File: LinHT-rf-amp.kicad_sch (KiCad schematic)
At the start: 22 parts, among them J1 Conn_Coaxial, J2 Conn_Coaxial, U1 GRF5604

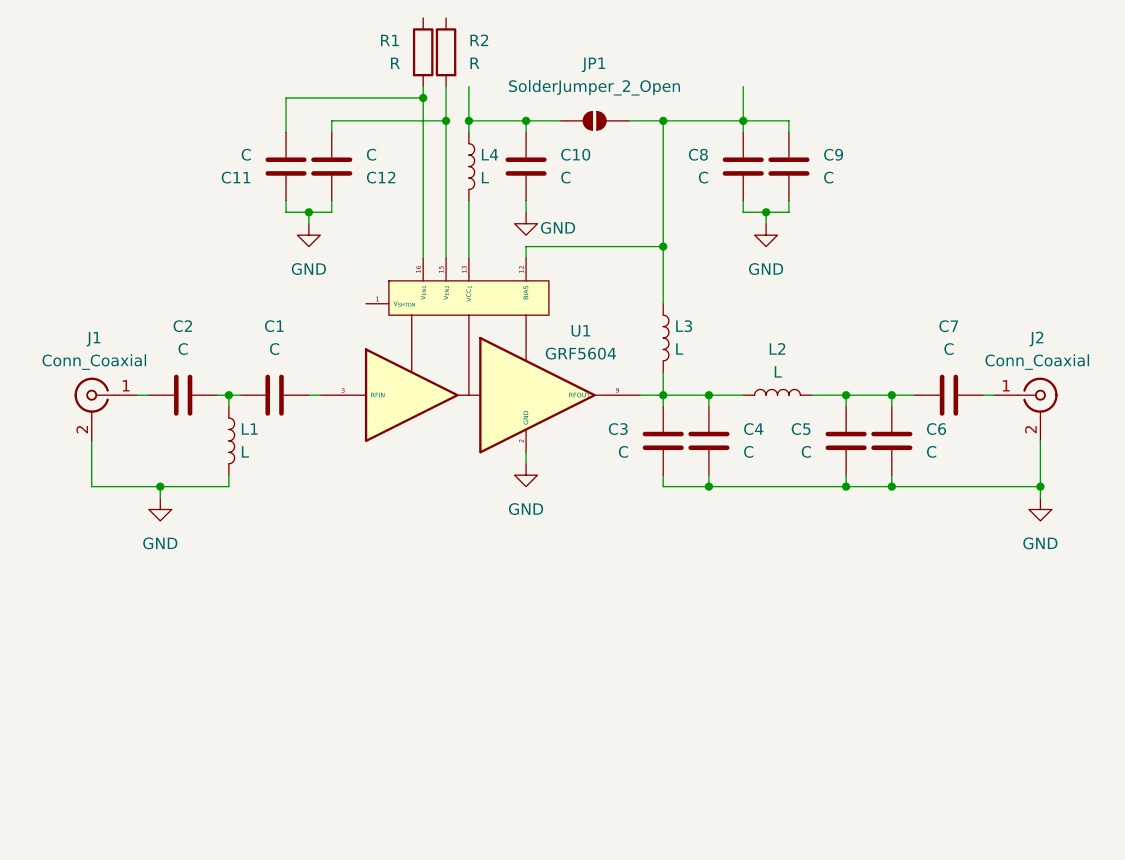
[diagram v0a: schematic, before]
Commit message: Added component values and connectors
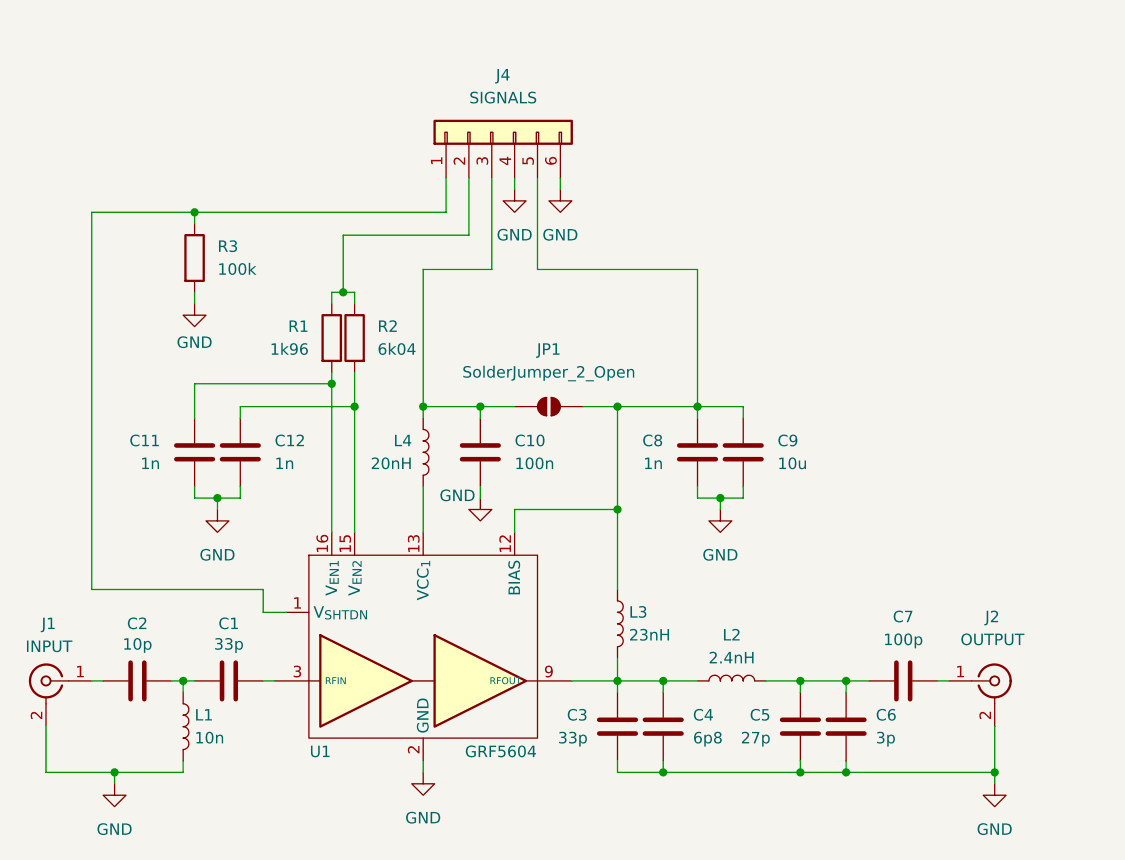
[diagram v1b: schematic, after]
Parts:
- added J4: SIGNALS, Connector_PinHeader_2.54mm:PinHeader_1x06_P2.54mm_Vertical, symbol Connector_Generic:Conn_01x06
- added R3: 100k, Resistor_SMD:R_0402_1005Metric, symbol Device:R
- C1, C3: value C -> 33p; footprint (none) -> Capacitor_SMD:C_0402_1005Metric
- C10: value C -> 100n; footprint (none) -> Capacitor_SMD:C_0402_1005Metric
- C11, C12, C8: value C -> 1n; footprint (none) -> Capacitor_SMD:C_0402_1005Metric
- C2: value C -> 10p; footprint (none) -> Capacitor_SMD:C_0402_1005Metric
- C4: value C -> 6p8; footprint (none) -> Capacitor_SMD:C_0402_1005Metric
- C5: value C -> 27p; footprint (none) -> Capacitor_SMD:C_0402_1005Metric
- C6: value C -> 3p; footprint (none) -> Capacitor_SMD:C_0402_1005Metric
- C7: value C -> 100p; footprint (none) -> Capacitor_SMD:C_0402_1005Metric
- C9: value C -> 10u; footprint (none) -> Capacitor_SMD:C_0402_1005Metric
- J1: value Conn_Coaxial -> INPUT; footprint (none) -> Connector_Coaxial:SMA_Amphenol_132289_EdgeMount
- J2: value Conn_Coaxial -> OUTPUT; footprint (none) -> Connector_Coaxial:SMA_Amphenol_132289_EdgeMount
- JP1: footprint (none) -> Jumper:SolderJumper-2_P1.3mm_Open_RoundedPad1.0x1.5mm
- L1: value L -> 10n; footprint (none) -> Inductor_SMD:L_0402_1005Metric
- L2: value L -> 2.4nH; footprint (none) -> Inductor_SMD:L_0603_1608Metric
- L3: value L -> 23nH
- L4: value L -> 20nH; footprint (none) -> Inductor_SMD:L_0402_1005Metric
- R1: value R -> 1k96; footprint (none) -> Resistor_SMD:R_0402_1005Metric
- R2: value R -> 6k04; footprint (none) -> Resistor_SMD:R_0402_1005Metric
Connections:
- net GND: now also J4.4 (Pin_4), J4.6 (Pin_6), R3.2
- net at R2.1: now also R1.1, J4.2 (Pin_2)
- net at C8.2, C9.2, JP1.2 (B)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: now also J4.5 (Pin_5)
- net at C10.2, JP1.1 (A), L4.1: now also J4.3 (Pin_3)
- net at U1.1 (V_{SHTDN}): now also J4.1 (Pin_1), R3.1
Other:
- company: (none) -> M17 Foundation
- title: (none) -> LinHT - 390-470 MHz Power Amplifier
- moved on the sheet: C1, C10, C11, C12, C2, C3, C4, C5, C6, C7, C8, C9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
